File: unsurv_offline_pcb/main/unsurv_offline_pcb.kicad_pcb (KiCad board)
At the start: 2 copper layers, 35 x 50 mm, 38 parts, among them J1 10103594-0001LF, J2 S2B-PH-SM4-TB_LF__SN_, J3 1.27mm_female_connector, Q1 UMH3N, U1 MCP73831-2-OT, U2 NCP59800, U3 APX803L20, U4 MPU-6050_NRND, U5 ESP32-WROOM-32, U6 CH340G, U7 ublox_SAM-M8Q

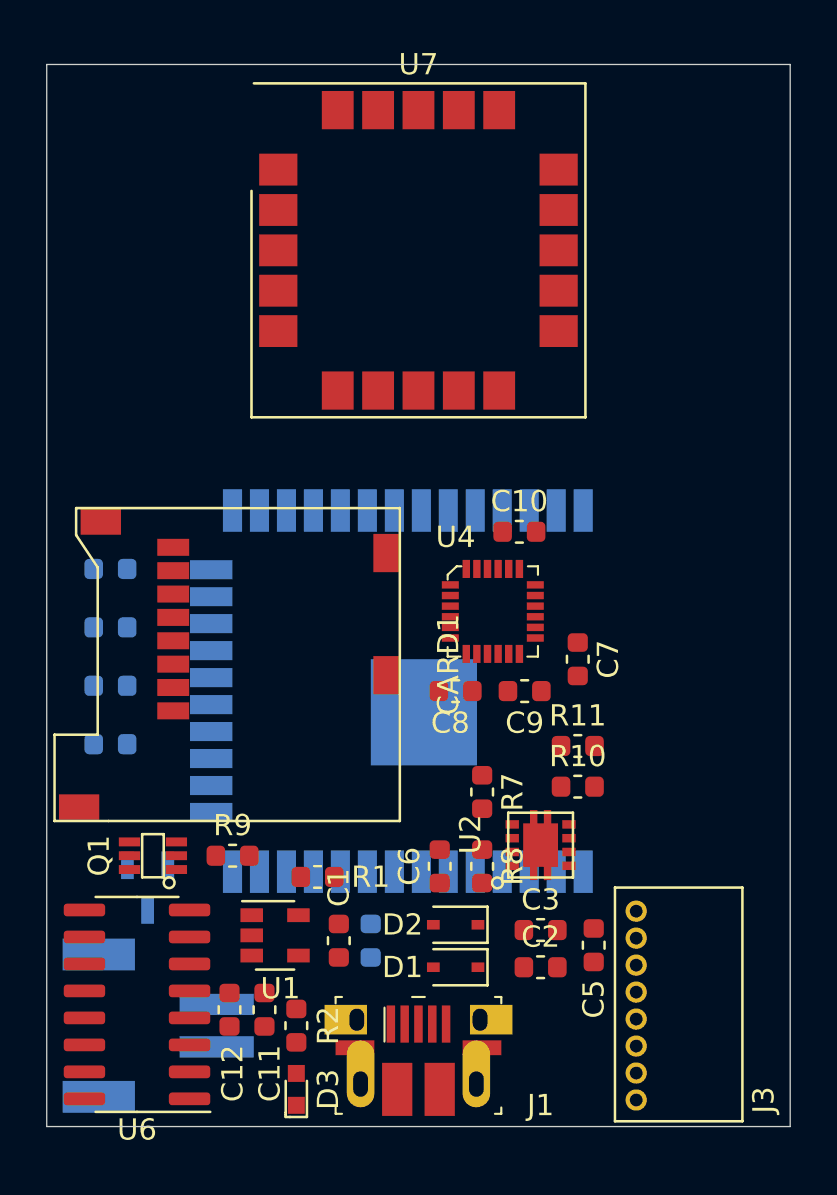
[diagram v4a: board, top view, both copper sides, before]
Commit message: created small pcb with 4 layers
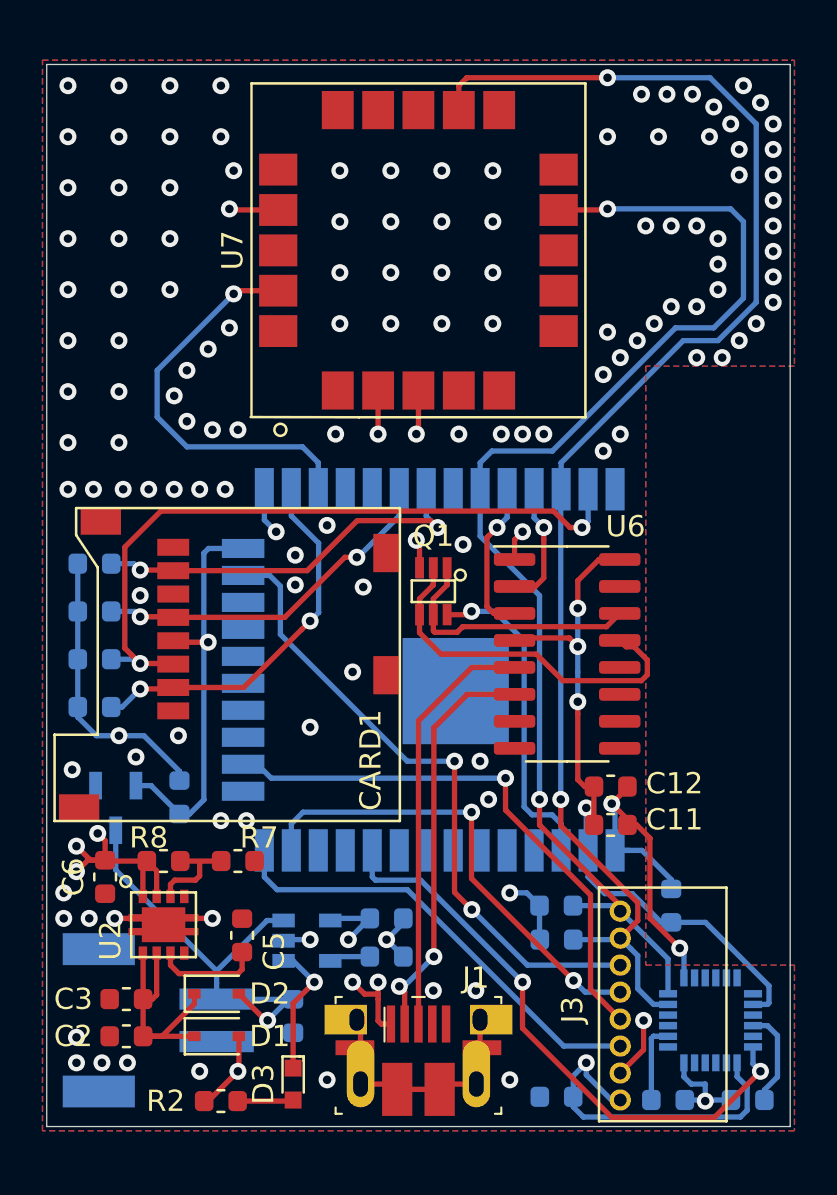
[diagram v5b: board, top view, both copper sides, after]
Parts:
- C1, C10, C7, C8, C9, R1, R10, R11, R9, U1, U4: moved to B.Cu
- moved C10 27.7 mm to (104.2, 123.8)
- moved U6 26.1 mm to (99.5, 102.8), turned to 0 degrees
- moved C9 21.9 mm to (108.0, 123.8), turned to 180 degrees
- moved U4 21.8 mm to (106.2, 120.0), turned to 270 degrees
- moved C12 20.8 mm to (101.5, 109.0), turned to 0 degrees
- moved C7 20.6 mm to (99.0, 123.6), turned to 180 degrees
- moved C2 19.8 mm to (78.8, 120.8), turned to 180 degrees
- moved C3 19.8 mm to (78.8, 119.0), turned to 180 degrees
- moved C11 18.5 mm to (101.5, 110.8), turned to 0 degrees
- moved Q1 18.1 mm to (93.2, 99.8), turned to 180 degrees
- moved U2 18.1 mm to (80.5, 115.5), turned to 0 degrees
- moved C5 16.6 mm to (84.2, 116.0), turned to 90 degrees
- moved C6 15.8 mm to (77.8, 113.2), turned to 270 degrees
- moved R8 15.0 mm to (80.5, 112.5), turned to 180 degrees
- moved C8 14.3 mm to (104.4, 114.6), turned to 270 degrees
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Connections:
- J3 pad 7: SDA -> SCL
- J3 pad 8: SCL -> SDA
- U5 pad 28: 17 -> Net-(U5-Pad28)
- U7 pad 13: 16 -> Net-(U7-Pad13)
- U7 pad 14: 17 -> Net-(U7-Pad14)
- U7 pad 19: 19 -> 16
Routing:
- net +3V3: track 0.00 -> 84.3 mm, vias 0 -> 14
- net SCL: track 0.00 -> 68.0 mm, vias 0 -> 2
- net SDA: track 0.00 -> 59.2 mm, vias 0 -> 2
- net GND: track 0.00 -> 35.7 mm, vias 0 -> 134
- net 23: track 0.00 -> 33.3 mm, vias 0 -> 2
- net 15: track 0.00 -> 30.3 mm, vias 0 -> 2
- net ACC_INT: track 0.00 -> 27.7 mm, vias 0 -> 2
- net 13: track 0.00 -> 26.2 mm, vias 0 -> 1
- net 14: track 0.00 -> 22.3 mm, vias 0 -> 2
- net 12: track 0.00 -> 21.3 mm
- net +BATT: track 0.00 -> 21.3 mm, vias 0 -> 1
- net D+: track 0.00 -> 19.8 mm
- net D-: track 0.00 -> 19.3 mm, vias 0 -> 2
- net 16: track 0.00 -> 19.2 mm, vias 0 -> 1
- net 19: track 0.00 -> 18.6 mm, vias 0 -> 2
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- added copper zone on PWR, net +3V3
- added copper zone on PWR, net +5V
- added copper zone on B.Cu, net GND
- added copper zone on F.Cu, net GND
- added copper zone on GND, net GND
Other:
- copper layers 2 -> 4

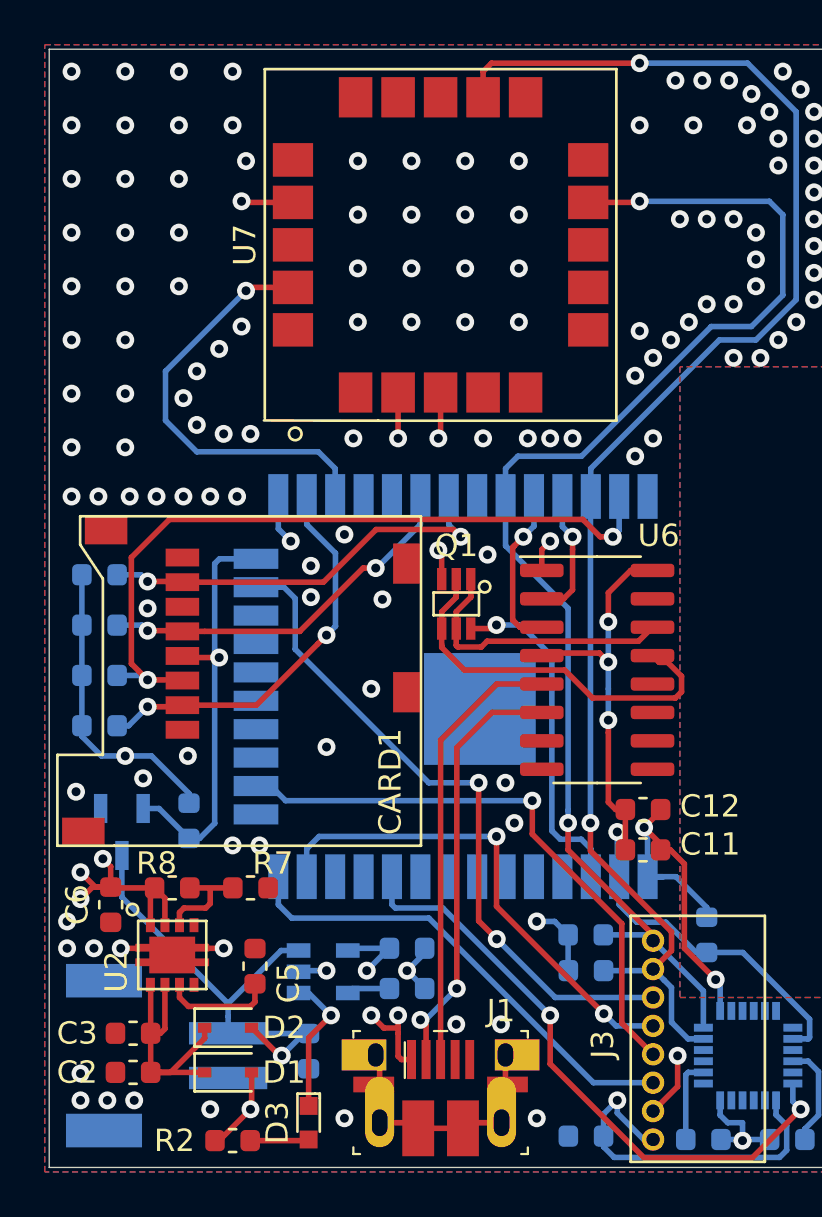
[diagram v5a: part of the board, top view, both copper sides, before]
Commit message: added addressable LED
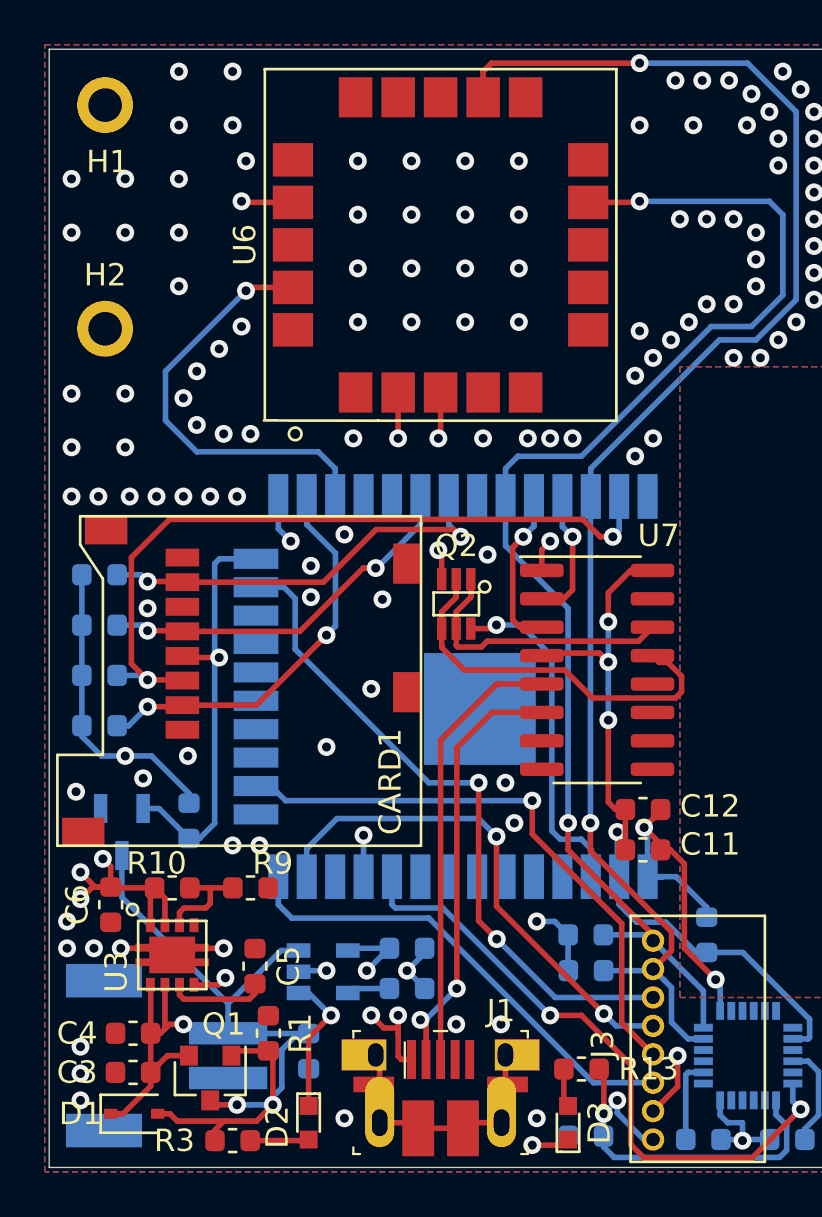
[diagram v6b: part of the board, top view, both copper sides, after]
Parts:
- removed the D2 at (83.0, 118.8)
- added D3: LED, digikey-footprints:LED_0603, F.Cu at (98.2, 123.0)
- added H1: MountingHole_Pad, MountingHole:MountingHole_2.2mm_M2_Pad, F.Cu at (77.5, 77.5)
- added H2: MountingHole_Pad, MountingHole:MountingHole_2.2mm_M2_Pad, F.Cu at (77.5, 87.5)
- added Q1: Q_PMOS_GSD, Package_TO_SOT_SMD:SOT-23, F.Cu at (82.2, 121.0)
- added R1: 10k, Resistor_SMD:R_0603_1608Metric, F.Cu at (84.8, 119.0)
- added R13: 2k, Resistor_SMD:R_0603_1608Metric, F.Cu at (98.8, 120.6)
- moved D1 4.59 mm to (78.8, 122.6)
- renumbered C4 to C2, C2 to C3, C3 to C4, D3 to D2, Q1 to Q2, R8 to R10, R10 to R11, R11 to R12, R1 to R2, R2 to R3, R3 to R4, R4 to R5, R5 to R6, R6 to R7, R9 to R8, R7 to R9, U3 to U2, U2 to U3, U7 to U6, U6 to U7
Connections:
- net Net-(U5-Pad12) renamed 27
- net Net-(U5-Pad29) renamed 5
- U5 pad 11: Net-(U5-Pad11) -> 26
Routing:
- net 26: track 0.00 -> 22.2 mm, vias 0 -> 2
- net +5V: track 11.1 -> 18.3 mm
- net Net-(C3-Pad1): track 12.6 -> 16.9 mm, vias 0 -> 2
- net +BATT: track 21.3 -> 24.7 mm
- net +3V3: track 84.3 -> 86.3 mm, vias 14 -> 15
- net Net-(D3-Pad2): track 0.00 -> 1.73 mm
- net ACC_INT: track 27.7 -> 28.5 mm
- net 14: track 22.3 -> 23.0 mm
- net Net-(C5-Pad1): track 5.00 -> 4.44 mm
- net GND: vias 134 -> 124

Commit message: pcb work
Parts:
- added C6: 100nF, Capacitor_SMD:C_0603_1608Metric, F.Cu at (97.2, 113.2)
- added R8: 10k, Resistor_SMD:R_0603_1608Metric, F.Cu at (95.6, 112.8)
- added RESET1: 2x2_switch, unsurv_offline_pcb_footprints:2x2 Switch, F.Cu at (90.0, 113.8)
- U6: footprint RF_GPS:ublox_SAM-M8Q -> RF_GPS:ublox_SAM-M8Q_HandSolder
- moved U6 0.40 mm to (92.5, 84.2)
- renumbered C9 to C10, C10 to C11, C11 to C12, C12 to C13, C6 to C7, C7 to C8, C8 to C9, R9 to R10, R10 to R11, R11 to R12, R12 to R13, R13 to R14, R8 to R9
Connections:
- net EN renamed RESET
- U4 pad 11: Net-(U4-Pad11) -> GND
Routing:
- net RESET: track 15.4 -> 23.7 mm, vias 1 -> 2
- net GND: track 35.7 -> 39.4 mm, vias 124 -> 129
- net 15: track 30.3 -> 32.4 mm
- net SCL: track 68.0 -> 69.9 mm
- net D-: track 19.3 -> 21.2 mm
- net D+: track 19.8 -> 21.2 mm
- net Net-(C10-Pad1): track 4.63 -> 5.29 mm
- net +3V3: track 86.3 -> 85.8 mm, vias 15 -> 16
- net (no net): vias 0 -> 3

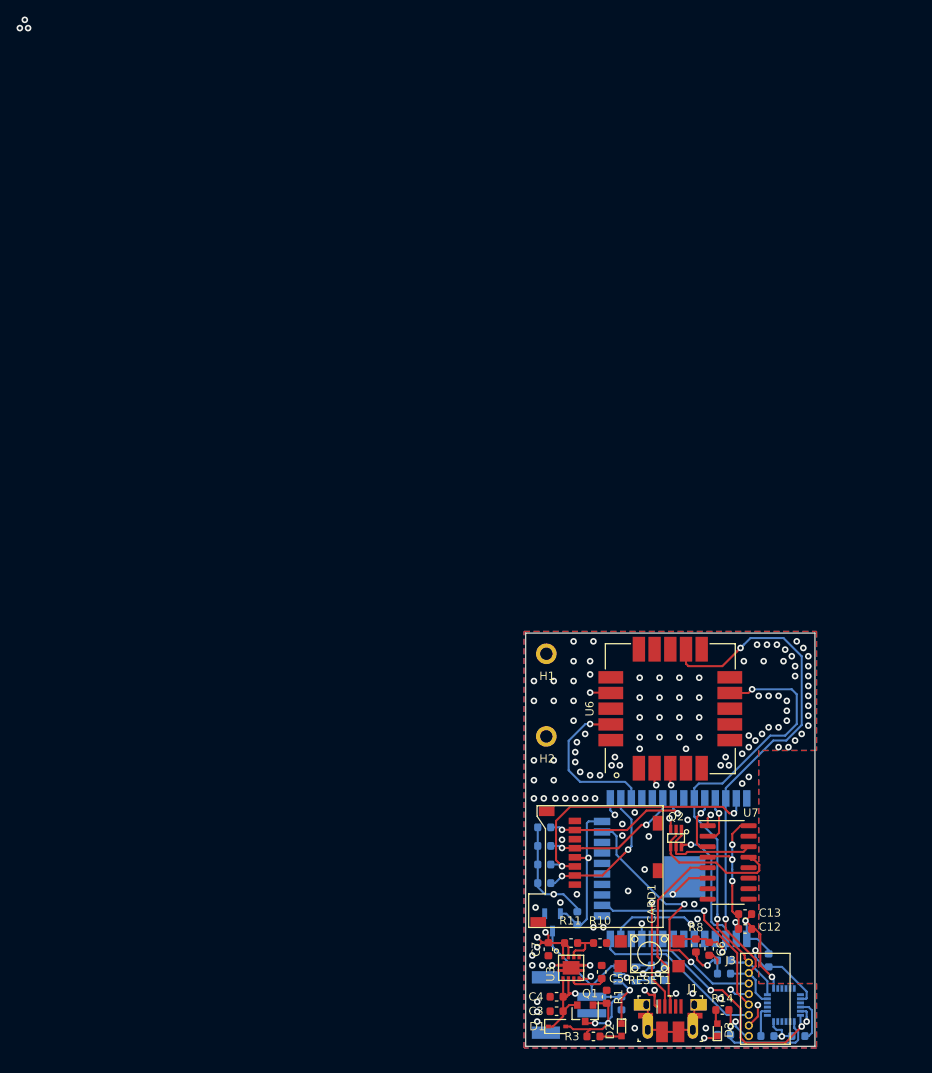
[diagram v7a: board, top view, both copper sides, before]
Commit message: added testpoints
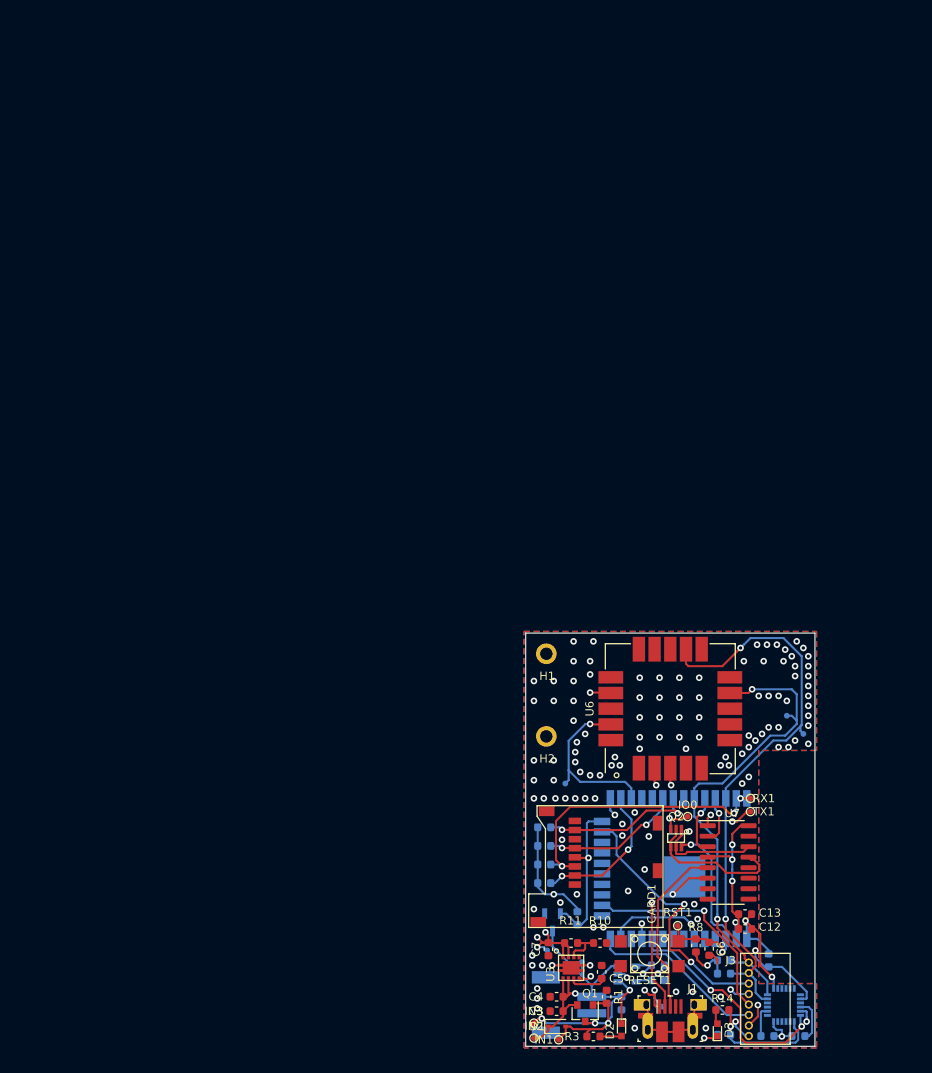
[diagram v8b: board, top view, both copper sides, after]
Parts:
- added 3V3: TestPoint, unsurv_offline_pcb_footprints:TestPoint_Pad_D0.7mm, B.Cu at (77.6, 113.4)
- added 5V1: TestPoint, unsurv_offline_pcb_footprints:TestPoint_Pad_D0.7mm, B.Cu at (91.6, 120.2)
- added BAT1: TestPoint, unsurv_offline_pcb_footprints:TestPoint_Pad_D0.7mm, B.Cu at (81.8, 114.8)
- added GINT1: TestPoint, unsurv_offline_pcb_footprints:TestPoint_Pad_D0.7mm, B.Cu at (79.8, 93.2)
- added IN1: TestPoint, unsurv_offline_pcb_footprints:TestPoint_Pad_D0.7mm, F.Cu at (79.0, 124.2)
- added IN2: TestPoint, unsurv_offline_pcb_footprints:TestPoint_Pad_D0.7mm, F.Cu at (76.0, 124.0)
- added IN3: TestPoint, unsurv_offline_pcb_footprints:TestPoint_Pad_D0.7mm, F.Cu at (76.0, 122.2)
- added IO0: TestPoint, unsurv_offline_pcb_footprints:TestPoint_Pad_D0.7mm, F.Cu at (94.6, 97.2)
- added RST1: TestPoint, unsurv_offline_pcb_footprints:TestPoint_Pad_D0.7mm, F.Cu at (93.4, 110.4)
- added RX1: TestPoint, unsurv_offline_pcb_footprints:TestPoint_Pad_D0.7mm, F.Cu at (102.2, 95.0)
- added SCL1: TestPoint, unsurv_offline_pcb_footprints:TestPoint_Pad_D0.7mm, B.Cu at (108.6, 87.2)
- added SDA1: TestPoint, unsurv_offline_pcb_footprints:TestPoint_Pad_D0.7mm, B.Cu at (106.6, 85.0)
- added TX1: TestPoint, unsurv_offline_pcb_footprints:TestPoint_Pad_D0.7mm, F.Cu at (102.2, 96.6)
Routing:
- net +BATT: track 24.7 -> 34.2 mm, vias 1 -> 2
- net RX0: track 7.35 -> 14.1 mm, vias 1 -> 2
- net TX0: track 5.90 -> 10.8 mm, vias 1 -> 2
- net +5V: track 18.3 -> 22.7 mm
- net Net-(C3-Pad1): track 16.9 -> 19.5 mm
- net 0: track 10.4 -> 12.7 mm
- net RESET: track 23.7 -> 25.7 mm
- net 16: track 19.3 -> 21.0 mm
- net SDA: track 58.7 -> 60.2 mm
- net +3V3: track 85.8 -> 87.2 mm
- net SCL: track 69.9 -> 71.2 mm
- net GND: vias 129 -> 127
- net (no net): vias 3 -> 0
